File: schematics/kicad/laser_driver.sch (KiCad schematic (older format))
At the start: 28 parts, among them Q3 BC547, Q4 BC547, Q5 BD237, Q6 MOSFET_N, U2 LM358, U5 LM339

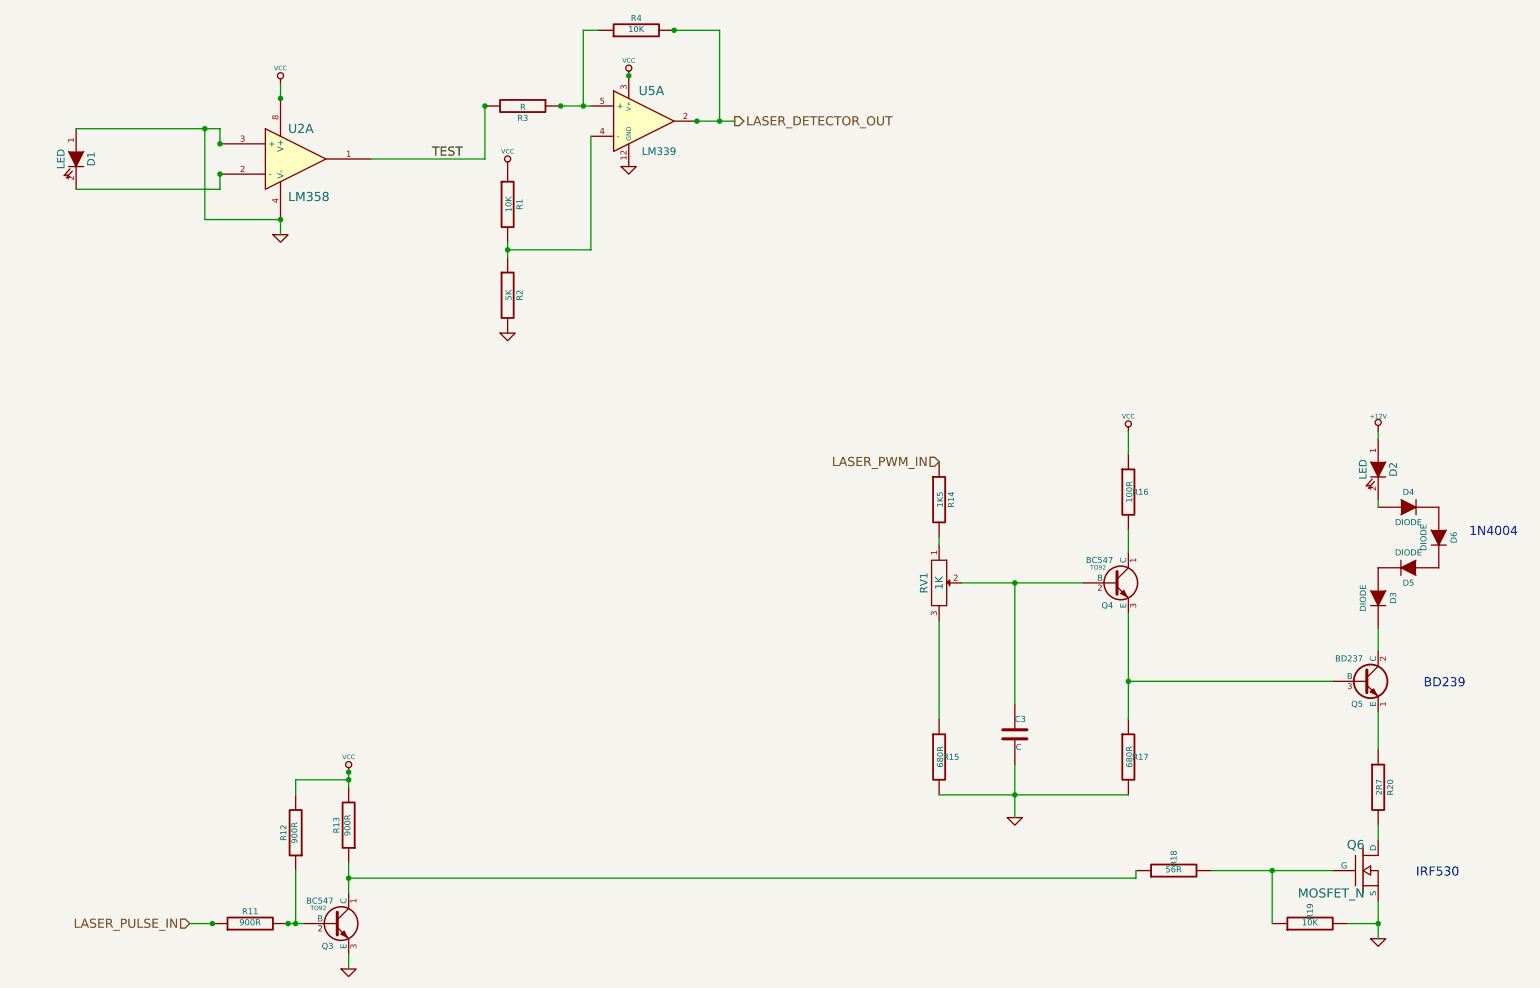
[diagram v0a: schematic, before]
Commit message: Finished schematics for initial prototype
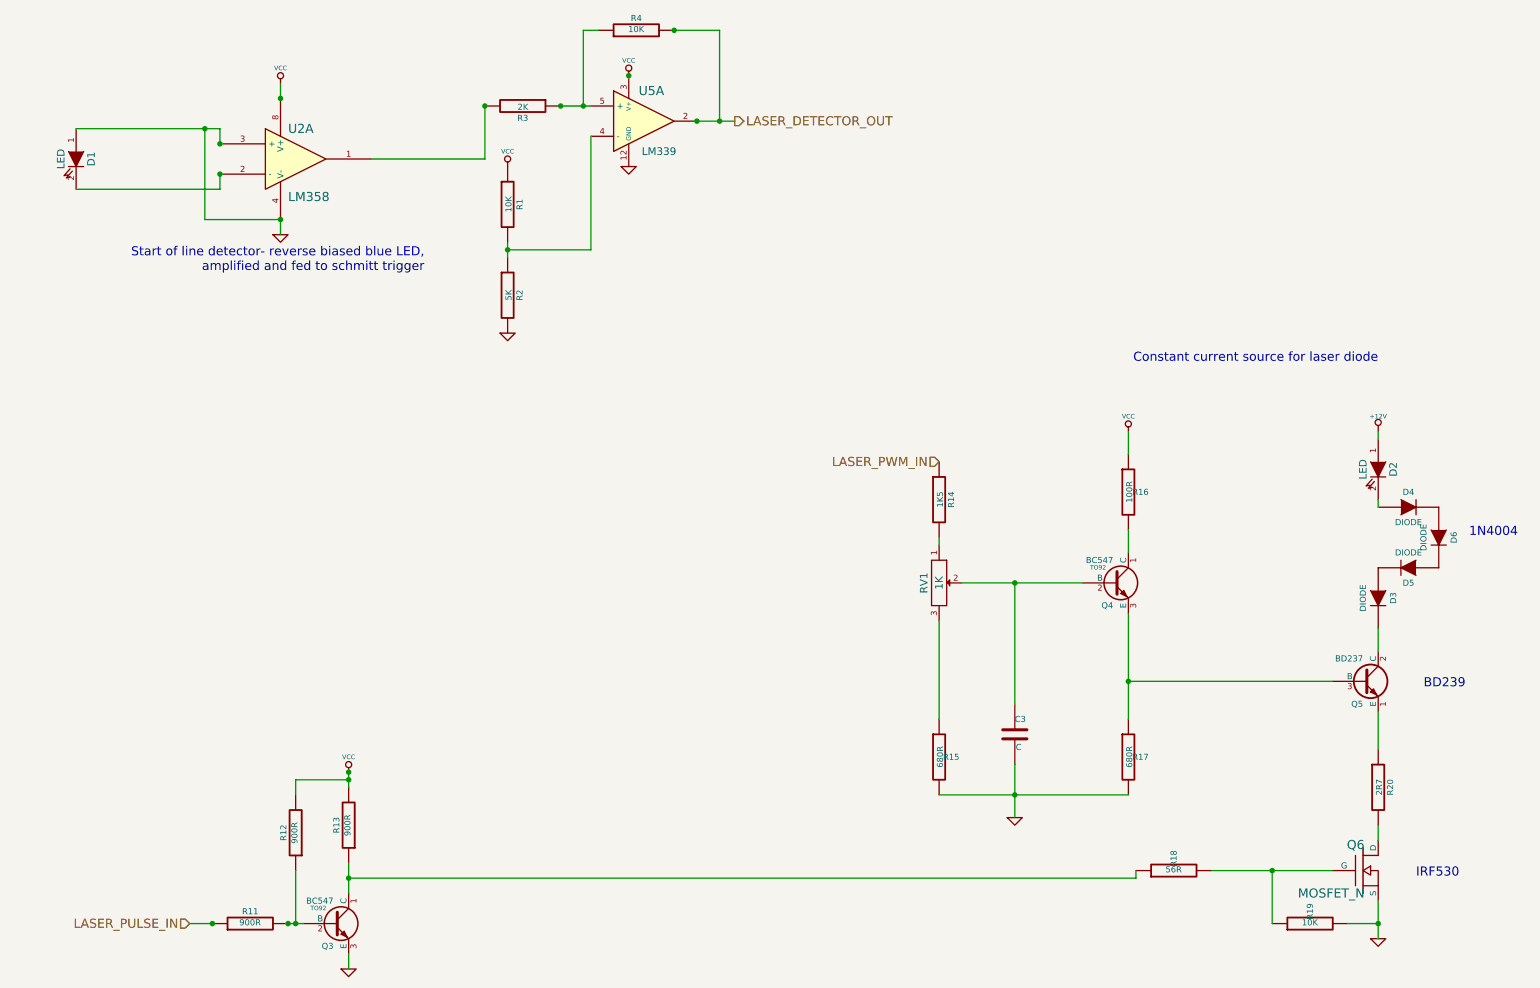
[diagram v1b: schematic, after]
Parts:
- R3: value R -> 2K
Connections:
- net TEST: no longer names the net of R3.2, U2.1
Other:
- note added: "Constant current source for laser diode\n"
- note added: "Start of line detector- reverse biased blue LED,\n amplified and fed to schmitt trigger\n"
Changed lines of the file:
@@
-EESchema Schematic File Version 2  date trešdiena, 2013. gada  1. maijs, plkst. 00 un 49
+EESchema Schematic File Version 2  date trešdiena, 2013. gada  1. maijs, plkst. 01 un 16
 LIBS:power
 LIBS:device
@@
 Wire Wire Line
 	8350 6550 8350 6500
-Text Label 3700 1800 0    60   ~ 0
-TEST
 Connection ~ 5450 1550
 Connection ~ 4550 1450
@@
 P 4300 1450
 F 0 "R3" V 4380 1450 40  0000 C CNN
-F 1 "R" V 4307 1451 40  0000 C CNN
+F 1 "2K" V 4307 1451 40  0000 C CNN
 F 2 "~" V 4230 1450 30  0000 C CNN
 F 3 "~" H 4300 1450 30  0000 C CNN
@@
 LASER_DETECTOR_OUT
 Connection ~ 5600 1550
+Text Notes 9950 3150 2    60   ~ 0
+Constant current source for laser diode\n
+Text Notes 3650 2550 2    60   ~ 0
+Start of line detector- reverse biased blue LED,\n amplified and fed to schmitt trigger\n
 $EndSCHEMATC
